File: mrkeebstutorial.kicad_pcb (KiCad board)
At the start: 2 copper layers, 309.6 x 100 mm, 153 parts, among them J1 USB_B_Mini, SW1 tilde/esc, SW10 9, SW11 0, SW12 _, SW13 =/+, SW14 Backspace_200, SW15 M1, SW16 Tab_150, SW17 Q, SW18 W, SW19 E, SW2 1, SW20 R, SW21 T, SW22 Y, SW23 U, SW24 I, SW25 O, SW26 P, SW27 {, SW28 }, SW29 \, SW3 2, SW30 M2, SW31 Caps, SW32 A, SW33 S, SW34 D, SW35 F, SW36 G, SW37 H, SW38 J, SW39 K, SW4 3, SW40 L, SW41 :, SW42 ", SW43 Enter_2.25, SW44 M3, SW45 LShift_225, SW46 z, SW47 x, SW48 c, SW49 v, SW5 4, SW50 b, SW51 n, SW52 m, SW53 <, SW54 >, SW55 ?, SW56 R-shift_175, SW57 UP, SW58 M4, SW59 LCTRL, SW6 5, SW60 Win, SW61 Alt, SW62 Space, SW63 Alt, SW64 Win, SW65 Menu, SW66 LEFT, SW67 DOWN, SW68 RIGHT, SW7 6, SW8 7, SW9 8, U1 ATmega32U4-AU, Y1 16MHz

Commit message: routed second thing
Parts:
- moved R2 87.0 mm to (-369.3, -327.1), turned to 90 degrees
- moved SWP1 83.9 mm to (-372.0, -332.4), turned to 0 degrees
- moved C5 77.0 mm to (-371.4, -327.7), turned to 90 degrees
- moved R1 71.4 mm to (-373.6, -327.1), turned to 90 degrees
- moved C8 66.1 mm to (-383.9, -312.5)
- moved C2 53.6 mm to (-417.9, -319.1), turned to 90 degrees
- moved C3 48.8 mm to (-415.5, -319.1), turned to 90 degrees
- moved C4 44.1 mm to (-413.2, -319.1), turned to 90 degrees
- moved C1 39.3 mm to (-410.8, -319.1), turned to 90 degrees
- moved R5 34.5 mm to (-408.4, -319.1)
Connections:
- U1 pad 1: Net-(U1-Pad1) -> Col5
- U1 pad 12: Col1 -> Row5
- U1 pad 18: Col7 -> Row4
- U1 pad 19: Col6 -> Row3
- U1 pad 20: Col5 -> Net-(U1-Pad20)
- U1 pad 21: Row3 -> Col1
- U1 pad 36: Net-(U1-Pad36) -> Row2
- U1 pad 40: Row2 -> Col7
- U1 pad 41: Net-(U1-Pad41) -> Col6
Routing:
- net Col7: track 68.7 -> 179.8 mm
- net Net-(U1-Pad41): track 107.3 -> 0.00 mm
- net Net-(U1-Pad42): track 107.4 -> 0.28 mm
- net Col6: track 69.6 -> 160.9 mm
- net Col5: track 67.2 -> 136.1 mm
- net Row5: track 283.4 -> 334.8 mm, vias 0 -> 2
- net +5V: track 22.1 -> 73.2 mm, vias 0 -> 2
- net GND: track 33.4 -> 76.1 mm
- net Row4: track 276.3 -> 314.8 mm, vias 0 -> 2
- net Net-(C6-Pad1): track 9.39 -> 44.7 mm
- net Net-(R3-Pad1): track 0.00 -> 35.0 mm, vias 0 -> 2
- net Net-(R4-Pad1): track 0.00 -> 34.3 mm, vias 0 -> 2
- net Row1: track 289.4 -> 320.1 mm, vias 0 -> 4
- net Net-(C7-Pad1): track 11.0 -> 40.9 mm
- net Net-(R5-Pad2): track 0.00 -> 21.5 mm
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
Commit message: caps
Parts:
- moved C3 32.9 mm to (-384.5, -308.2), turned to 180 degrees
- moved R5 32.8 mm to (-375.7, -320.8), turned to 0 degrees
- moved C2 29.8 mm to (-389.5, -328.0), turned to 180 degrees
- moved C4 23.6 mm to (-393.7, -305.7), turned to 0 degrees
- moved C1 11.4 mm to (-399.9, -322.5), turned to 0 degrees
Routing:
- net +5V: track 73.2 -> 142.8 mm
- net Net-(R5-Pad2): track 21.5 -> 38.6 mm, vias 0 -> 2
- net GND: track 76.1 -> 63.1 mm, vias 0 -> 2
- net Net-(U1-Pad39): track 5.25 -> 0.00 mm

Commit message: i think done
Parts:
- SW16: moved to B.Cu
- moved C2 2.20 mm to (-387.8, -329.4), turned to 90 degrees
- turned R1 to 270 degrees
- turned SW16 to 180 degrees
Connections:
- U1 pad 10: Col4 -> Col3
- U1 pad 11: Net-(U1-Pad11) -> Col4
- U1 pad 13: RST -> Net-(U1-Pad13)
- U1 pad 36: Row2 -> Net-(U1-Pad36)
- U1 pad 37: Net-(U1-Pad37) -> RST
- U1 pad 8: Col2 -> Row2
- U1 pad 9: Col3 -> Col2
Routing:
- net Row2: track 266.9 -> 332.1 mm, vias 0 -> 7
- net GND: track 63.1 -> 115.6 mm, vias 2 -> 5
- net RST: track 4.81 -> 36.5 mm
- net Net-(J1-Pad6): track 0.00 -> 25.6 mm
- net +5V: track 142.8 -> 128.7 mm
- net Row1: track 320.1 -> 330.6 mm, vias 4 -> 2
- net Net-(D17-Pad2): track 0.00 -> 9.26 mm, vias 0 -> 1
- net Net-(D4-Pad2): track 0.00 -> 8.18 mm, vias 0 -> 1
- net Net-(C7-Pad1): track 40.9 -> 43.3 mm
- net Col13: track 321.4 -> 323.1 mm
- net Col2: track 122.6 -> 124.0 mm
- net Net-(C6-Pad1): track 44.7 -> 45.5 mm
- net Col4: track 139.9 -> 139.2 mm
- added copper zone on B.Cu, net GND

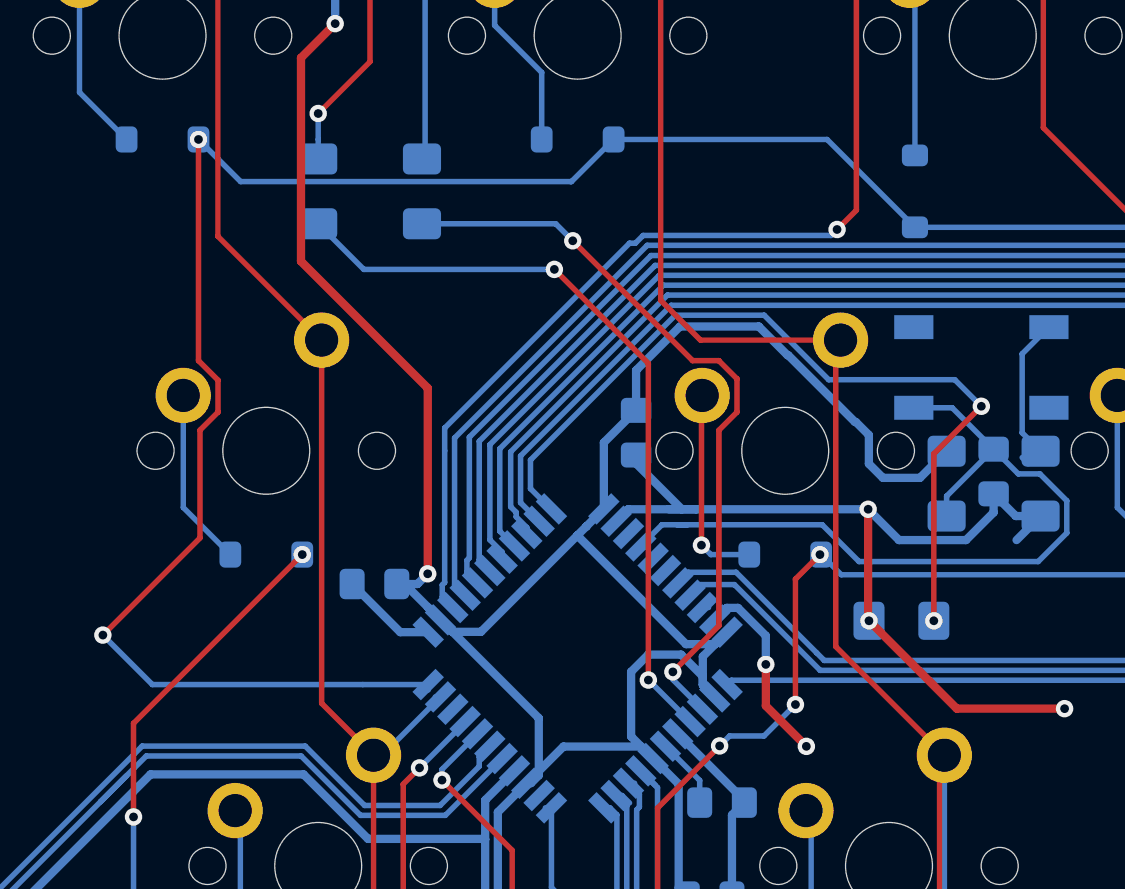
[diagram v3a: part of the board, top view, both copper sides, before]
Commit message: resolved vias under pads
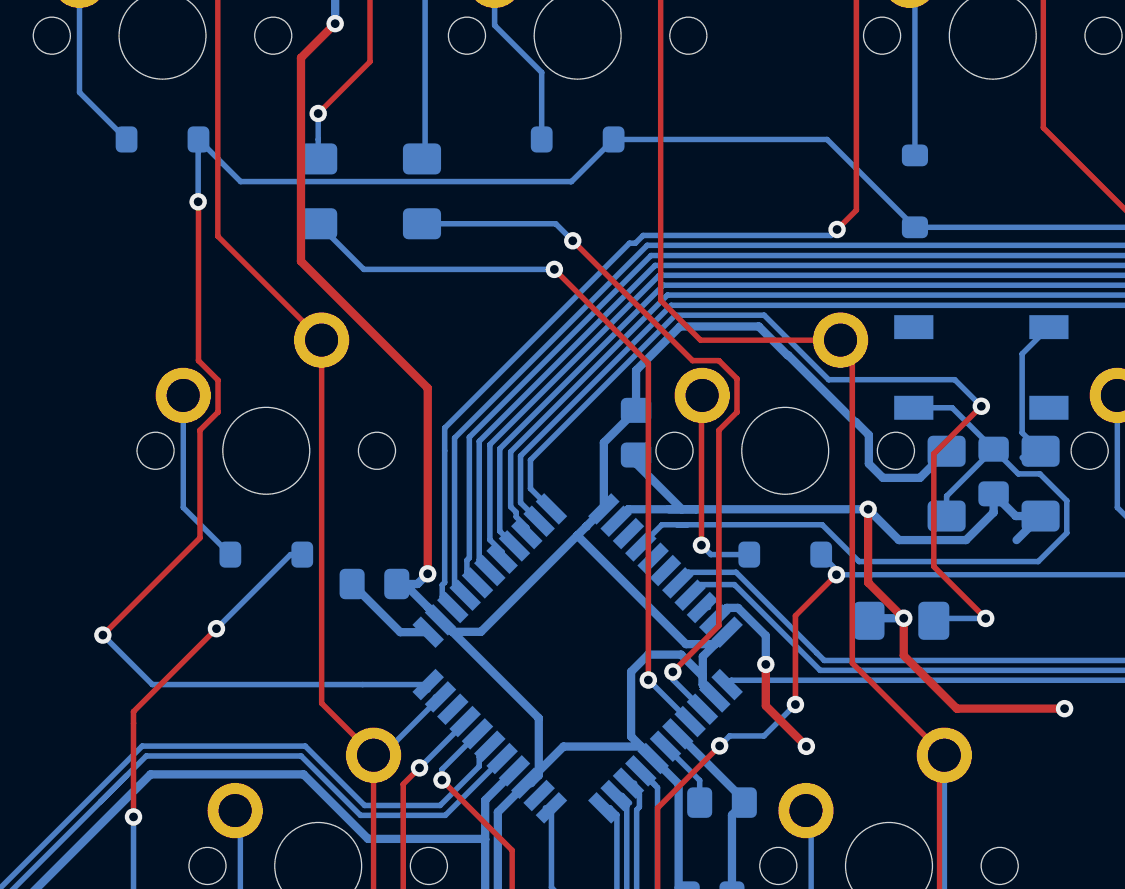
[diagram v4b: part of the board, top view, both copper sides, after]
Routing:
- net Net-(R5-Pad2): track 38.6 -> 41.9 mm
- net GND: track 115.6 -> 117.2 mm
